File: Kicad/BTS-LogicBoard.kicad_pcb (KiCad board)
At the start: 2 copper layers, 41.9 x 55.9 mm, 54 parts, among them J1 Conn_01x06, J2 Conn_01x04, J3 Conn_01x02, Q1 BC817, Q2 BC807, Q3 BC817, Q4 BC807, Q5 BC817, Q6 BC817, SW1 SW_DPDT_x2, SW2 SW_DPDT_x2, U1 NCS2252SN2T1G, U2 NE555D, U3 NCS2252SN2T1G, U4 TLP291

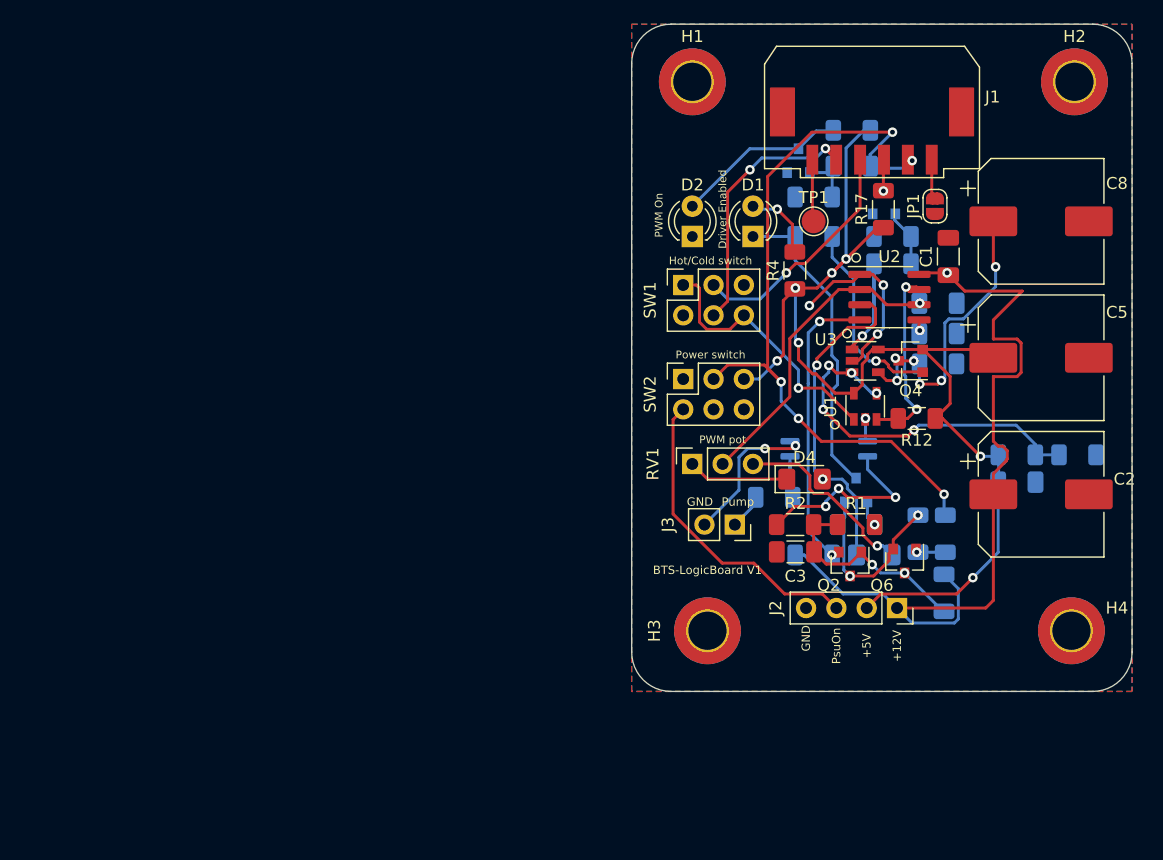
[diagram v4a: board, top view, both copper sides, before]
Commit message: Restarted layout
Signed-off-by: bebenlebricolo <benoittarrade@hotmail.fr>
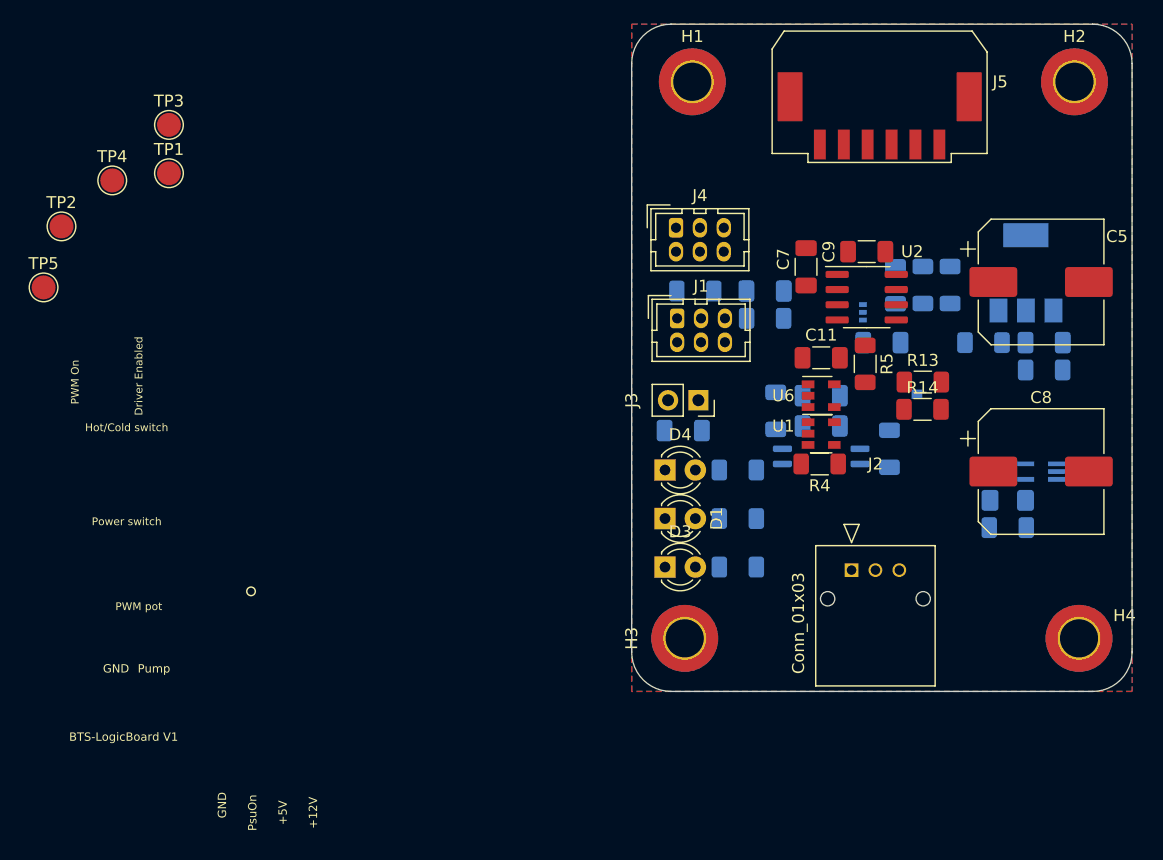
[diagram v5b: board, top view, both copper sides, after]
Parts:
- removed C1: 1uF, Capacitor_SMD:C_1206_3216Metric_Pad1.33x1.80mm_HandSolder
- removed C2: 470uF, Capacitor_SMD:CP_Elec_10x10
- removed JP1: SolderJumper_2_Open, Jumper:SolderJumper-2_P1.3mm_Open_RoundedPad1.0x1.5mm
- removed Q2, Q4: BC807, Package_TO_SOT_SMD:SOT-23
- removed Q3, Q5, Q6: BC817, Package_TO_SOT_SMD:SOT-23
- removed R17, R18: 1k, Resistor_SMD:R_1206_3216Metric_Pad1.30x1.75mm_HandSolder
- removed R19: 56k, Resistor_SMD:R_1206_3216Metric_Pad1.30x1.75mm_HandSolder
- removed RV1: R_POT, Connector_PinSocket_2.54mm:PinSocket_1x03_P2.54mm_Vertical
- removed SW1, SW2: SW_DPDT_x2, BTS-LogicBoard:PinSocket_2x03_P2.54mm_Vertical_DPDT_Special
- added C10: 100nF, Capacitor_SMD:C_1206_3216Metric_Pad1.33x1.80mm_HandSolder, B.Cu at (127.6, 99.7)
- added C11: 100nF, Capacitor_SMD:C_1206_3216Metric_Pad1.33x1.80mm_HandSolder, F.Cu at (127.6, 94.0)
- added C12: 100nF, Capacitor_SMD:C_1206_3216Metric_Pad1.33x1.80mm_HandSolder, B.Cu at (127.6, 97.2)
- added C13: 1uF, Capacitor_SMD:C_1206_3216Metric_Pad1.33x1.80mm_HandSolder, B.Cu at (122.9, 88.4)
- added C9: 100nF, Capacitor_SMD:C_1206_3216Metric_Pad1.33x1.80mm_HandSolder, F.Cu at (131.4, 85.1)
- added J4: Conn_02x03_Odd_Even, Connector_Hirose:Hirose_DF11-6DP-2DSA_2x03_P2.00mm_Vertical, F.Cu at (115.5, 83.1)
- added J5: Conn_01x06, BTS-LogicBoard:Molex_MicroLock_1.25_01x06, F.Cu at (136.5, 71.1)
- added TP2: TestPoint, TestPoint:TestPoint_Pad_D2.0mm, F.Cu at (64.0, 83.0)
- added TP3: TestPoint, TestPoint:TestPoint_Pad_D2.0mm, F.Cu at (73.0, 74.5)
- added TP4: TestPoint, TestPoint:TestPoint_Pad_D2.0mm, F.Cu at (68.3, 79.1)
- added TP5: TestPoint, TestPoint:TestPoint_Pad_D2.0mm, F.Cu at (62.5, 88.1)
- added U5: 74HC1GU04, Package_TO_SOT_SMD:SOT-353_SC-70-5, B.Cu at (130.2, 90.2)
- added U6: NCS2252SN2T1G, Package_TO_SOT_SMD:SOT-23-5, F.Cu at (127.6, 97.2)
- added U8: LM1117-5.0, Package_TO_SOT_SMD:SOT-223-3_TabPin2, B.Cu at (144.8, 86.9)
- C3, R2: moved to B.Cu
- C7: value 10pF -> 220pF; moved to F.Cu
- D2: value LED -> 1N4148; footprint LED_THT:LED_D3.0mm -> Diode_SMD:D_1206_3216Metric_Pad1.42x1.75mm_HandSolder; moved to B.Cu
- D3: value 1N4148 -> LED; footprint Diode_SMD:D_1206_3216Metric_Pad1.42x1.75mm_HandSolder -> LED_THT:LED_D3.0mm; moved to F.Cu
- D4: value 1N4148 -> LED; footprint Diode_SMD:D_1206_3216Metric_Pad1.42x1.75mm_HandSolder -> LED_THT:LED_D3.0mm
- J1: value Conn_01x06 -> Conn_02x03_Odd_Even; footprint BTS-LogicBoard:Molex_MicroLock_1.25_01x06 -> Connector_Hirose:Hirose_DF11-6DP-2DSA_2x03_P2.00mm_Vertical
- J2: value Conn_01x04 -> Conn_01x03; footprint Connector_PinSocket_2.54mm:PinSocket_1x04_P2.54mm_Vertical -> BTS-LogicBoard:559350310
- R1, R12: value 1k -> 470; moved to B.Cu
- R13: moved to F.Cu
- R14: value 390k -> 56k; moved to F.Cu
- R15: value 1k -> 470
- R16, R8: value 56k -> 5.6k
- R3: value 56k -> 390k
- R4: value 470 -> 1k
- R5: value 56k -> 1k; moved to F.Cu
- R6: value 1k -> 220
- R7: value 1k -> 10k
- U2: value NE555D -> NE555DR/TS555
- U3: value NCS2252SN2T1G -> 74HC1GU04; footprint Package_TO_SOT_SMD:SOT-23-5 -> Package_TO_SOT_SMD:SOT-353_SC-70-5_Handsoldering; moved to B.Cu
- moved TP1 54.1 mm to (73.0, 78.5)
- moved R9 37.8 mm to (120.7, 111.5)
- moved D2 34.4 mm to (143.3, 105.9), turned to 0 degrees
- moved J1 27.3 mm to (115.6, 90.7), turned to 0 degrees
- moved D1 24.7 mm to (114.6, 107.4), turned to 0 degrees
- moved R6 24.4 mm to (136.1, 87.9), turned to 90 degrees
- moved R15 21.6 mm to (120.7, 103.4)
- moved C8 21.0 mm to (146.1, 103.5)
- moved R5 20.3 mm to (131.3, 94.5)
- moved D3 17.6 mm to (114.6, 111.5)
- moved U3 17.4 mm to (146.1, 103.5), turned to 180 degrees
- moved R4 16.3 mm to (127.5, 102.9), turned to 180 degrees
- moved R13 15.2 mm to (136.1, 96.0), turned to 0 degrees
- moved C3 13.8 mm to (116.1, 100.1)
- moved R7 12.9 mm to (138.4, 87.9), turned to 90 degrees
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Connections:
- C3 pad 1: GND -> GND1
- C3 pad 2: /PWM_Enable -> /EnableSignal
- C4 pad 1: +5V -> VCC
- C5 pad 1: +5V -> VCC
- D1 pad 1: /PWM_Enabled_INV -> Net-(D1-Pad1)
- D2 pad 1: GND -> Net-(C8-Pad1)
- D2 pad 2: Net-(D2-Pad2) -> Net-(D1-Pad2)
- D3 pad 1: Net-(D3-Pad1) -> GND
- D4 pad 2: Net-(D3-Pad1) -> Net-(D4-Pad2)
- J1 pad 1: /HIP_HEN -> /+Potentiometer
- J1 pad 2: /HIP_DISABLE -> /PSU_ON
- J1 pad 3: /FAN_TRIGGER -> /PWM_DCycle_Ref
- J1 pad 4: /IN+ -> GND
- J1 pad 5: /IN- -> /-Potentiometer
- J1 pad 6: /VSense -> GND
- J2 pad 1: +12V -> +5V
- J2 pad 2: +5V -> /PSU_ON
- J2 pad 3: /PSU_ON -> GND
- J3 pad 1: /Pump-On -> /EnableSignal
- Q1 pad 3: /PWM_Enabled_INV -> Net-(D4-Pad1)
- R1 pad 1: Net-(Q1-Pad1) -> GND
- R1 pad 2: /PWM_Enable -> Net-(D1-Pad1)
- R10 pad 1: +5V -> VCC
- R12 pad 1: +5V -> VCC
- R12 pad 2: /NE-Out -> Net-(R12-Pad2)
- R13 pad 1: Net-(Q4-Pad1) -> /COMP_PWM
- R13 pad 2: /PWM_Enabled_INV -> Net-(Q1-Pad1)
- R14 pad 2: Net-(C8-Pad1) -> Net-(Q1-Pad1)
- R15 pad 1: Net-(Q5-Pad1) -> VCC
- R15 pad 2: /Inv_Fan_trigger -> Net-(D4-Pad2)
- R16 pad 1: GND -> /-Potentiometer
- R16 pad 2: Net-(Q5-Pad1) -> GND
- R2 pad 1: /PWM_Enable -> VCC
- R2 pad 2: Net-(R2-Pad2) -> /EnabledOpto
- R20 pad 2: /Pump-On -> /EnableSignal
- R3 pad 2: Net-(Q1-Pad1) -> Net-(C8-Pad1)
- R4 pad 1: +5V -> VCC
- R4 pad 2: Net-(D1-Pad2) -> /COMP_PWM
- R5 pad 1: +12V -> VCC
- R5 pad 2: /PWM_Enable -> /FAN_TRIGGER
- R6 pad 1: +12V -> Net-(R12-Pad2)
- R6 pad 2: Net-(Q2-Pad2) -> /Threshold
- R7 pad 1: Net-(Q3-Pad1) -> /Sawtooth
- R7 pad 2: /HIP_DISABLE -> /Threshold
- R8 pad 1: GND -> VCC
- R8 pad 2: Net-(Q3-Pad1) -> /+Potentiometer
- R9 pad 1: +5V -> VCC
- R9 pad 2: Net-(D2-Pad2) -> Net-(D3-Pad2)
- TP1 pad 1: /VSense -> /NE_OUT
- U1 pad 1: /COMP-Out -> /COMP_PWM
- U1 pad 3: /NE-Out -> /Sawtooth
- U1 pad 4: /2.5V -> /PWM_DCycle_Ref
- U1 pad 5: +5V -> VCC
- U2 pad 3: Net-(D3-Pad1) -> /NE_OUT
- U2 pad 4: Net-(Q2-Pad2) -> /NE555_RST
- U2 pad 7: /NE-Out -> Net-(R12-Pad2)
- U2 pad 8: +12V -> VCC
- U3 pad 1: /Inv_Fan_trigger -> (no net)
- U3 pad 2: GND -> /EnabledOpto
- U3 pad 3: /2.5V -> GND
- U3 pad 4: Net-(C8-Pad1) -> Net-(D1-Pad2)
- U3 pad 5: +5V -> VCC
- U4 pad 4: Net-(R2-Pad2) -> /EnabledOpto
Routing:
- net +5V: track 95.1 -> 0.00 mm, vias 7 -> 0
- net +12V: track 70.4 -> 0.00 mm, vias 1 -> 0
- net /HIP_DISABLE: track 64.7 -> 0.00 mm, vias 5 -> 0
- net GND: track 32.6 -> 0.00 mm, vias 6 -> 0
- net /2.5V: track 31.5 -> 0.00 mm, vias 5 -> 0
- net Net-(D3-Pad1): track 27.8 -> 0.00 mm, vias 2 -> 0
- net /PWM_Enabled_INV: track 26.4 -> 0.00 mm
- net /PSU_ON: track 26.1 -> 0.00 mm
- net /Threshold: track 25.9 -> 0.00 mm, vias 1 -> 0
- net Net-(C8-Pad1): track 25.2 -> 0.00 mm, vias 6 -> 0
- net Net-(Q2-Pad2): track 24.9 -> 0.00 mm, vias 2 -> 0
- net /COMP-Out: track 22.5 -> 0.00 mm, vias 1 -> 0
- net /IN-: track 21.8 -> 0.00 mm, vias 2 -> 0
- net /IN+: track 20.0 -> 0.00 mm, vias 1 -> 0
- net /PWM_Enable: track 18.3 -> 0.00 mm, vias 2 -> 0
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
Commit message: Finalized layout for Version 1.1 (need to work on silkscreen now)
Signed-off-by: bebenlebricolo <benoittarrade@hotmail.fr>
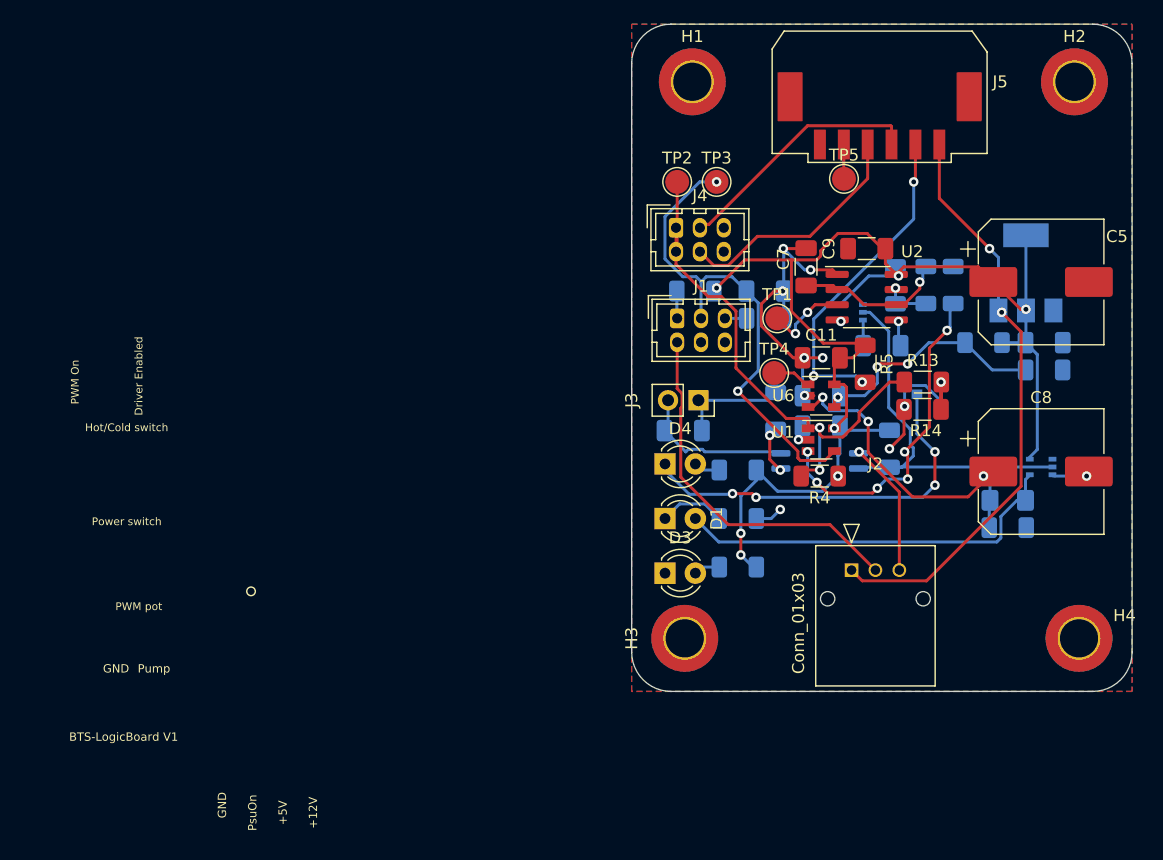
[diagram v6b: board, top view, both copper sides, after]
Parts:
- U3: footprint Package_TO_SOT_SMD:SOT-353_SC-70-5_Handsoldering -> Package_TO_SOT_SMD:SOT-353_SC-70-5
- moved TP5 67.6 mm to (129.5, 79.0)
- moved TP4 57.7 mm to (123.7, 95.2)
- moved TP1 52.4 mm to (124.0, 90.7)
- moved TP2 51.7 mm to (115.6, 79.2)
- moved TP3 46.1 mm to (118.9, 79.2)
- moved R4 1.02 mm to (127.5, 103.9)
- moved D3 0.51 mm to (114.6, 112.0)
- moved D4 0.51 mm to (114.6, 102.9)
- moved U1 0.51 mm to (127.6, 100.8)
- moved U4 0.40 mm to (127.5, 102.6)
- moved U3 0.38 mm to (146.1, 103.1)
- moved C6 0.25 mm to (132.7, 93.0)
- moved C9 0.25 mm to (131.4, 84.8)
- moved R6 0.25 mm to (136.4, 87.9)
- moved R7 0.25 mm to (138.7, 87.9)
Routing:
- net VCC: track 0.00 -> 108.6 mm, vias 0 -> 7
- net GND: track 0.00 -> 59.1 mm, vias 0 -> 12
- net +5V: track 0.00 -> 49.4 mm, vias 0 -> 2
- net /COMP_PWM: track 0.00 -> 45.3 mm, vias 0 -> 2
- net /PWM_DCycle_Ref: track 0.00 -> 41.1 mm, vias 0 -> 2
- net Net-(D1-Pad2): track 0.00 -> 33.1 mm
- net /EnabledOpto: track 0.00 -> 32.8 mm
- net Net-(D4-Pad1): track 0.00 -> 32.3 mm, vias 0 -> 4
- net /FAN_TRIGGER: track 0.00 -> 31.3 mm, vias 0 -> 3
- net /PSU_ON: track 0.00 -> 31.0 mm
- net /Sawtooth: track 0.00 -> 28.0 mm, vias 0 -> 6
- net Net-(C8-Pad1): track 0.00 -> 27.6 mm, vias 0 -> 3
- net /IN+: track 0.00 -> 21.1 mm
- net /IN-: track 0.00 -> 20.4 mm
- net /2.5V: track 0.00 -> 20.3 mm, vias 0 -> 3
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
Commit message: Finalized board layout with silkscreen
Signed-off-by: bebenlebricolo <benoittarrade@hotmail.fr>
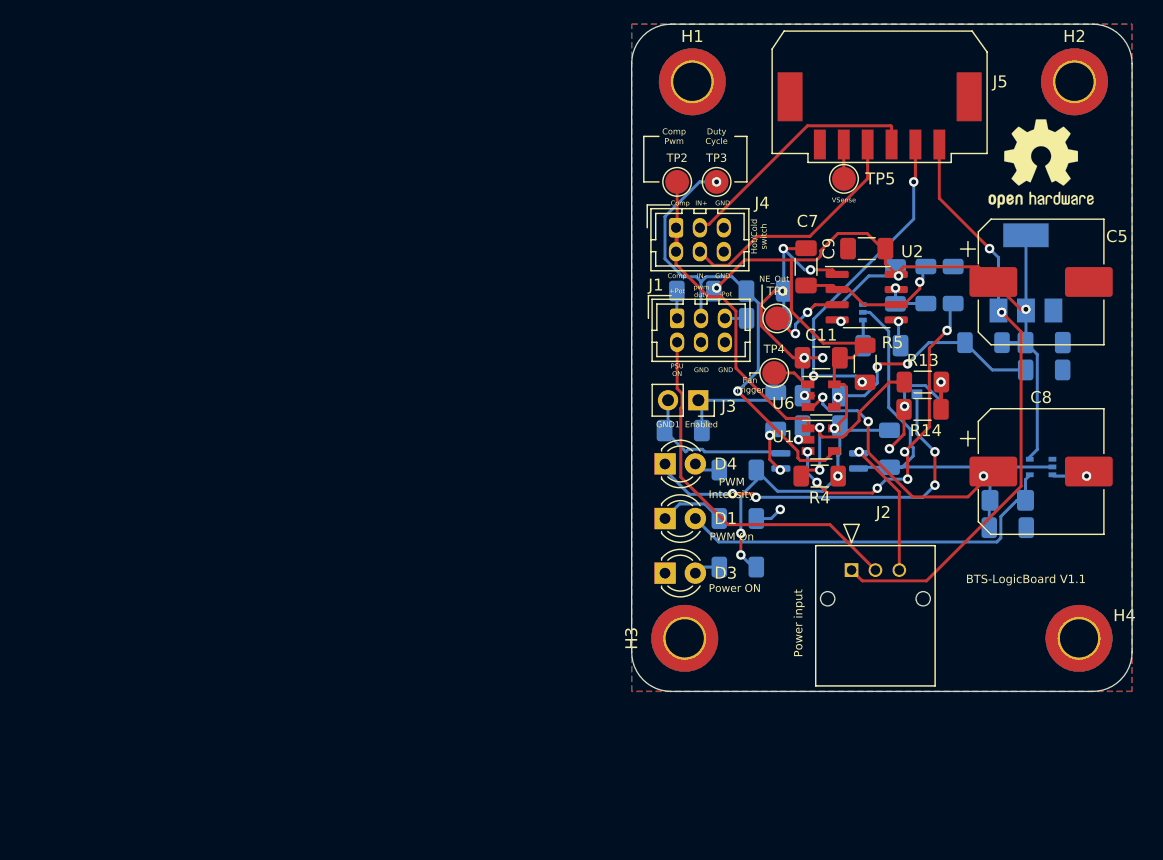
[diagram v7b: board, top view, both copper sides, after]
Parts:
- added REF**: OSHW-Logo2_9.8x8mm_SilkScreen, Symbol:OSHW-Logo2_9.8x8mm_SilkScreen, F.Cu at (146.1, 77.7)
- J2: value Conn_01x03 -> Power input
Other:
- board text added: "+Pot"
- board text added: "-Pot"
- board text added: "BTS-LogicBoard V1.1"
- board text added: "Comp"
- board text added: "Comp Pwm"
- board text added: "Duty Cycle"
- board text added: "Enabled"
- board text added: "Fan Trigger"
- board text added: "GND1"
- board text added: "IN+"
- board text added: "IN-"
- board text added: "NE_Out"
- board text added: "PSU ON"
- board text added: "PWM Intensity"
- board text added: "Power ON"
- board text added: "VSense"
- board text added: "pwm duty"
- board text removed: "+12V"
- board text removed: "+5V"
- board text removed: "BTS-LogicBoard V1"
- board text removed: "Driver Enabled"
- board text removed: "PWM pot"
- board text removed: "Power switch"
- board text removed: "PsuOn"
- board text removed: "Pump"

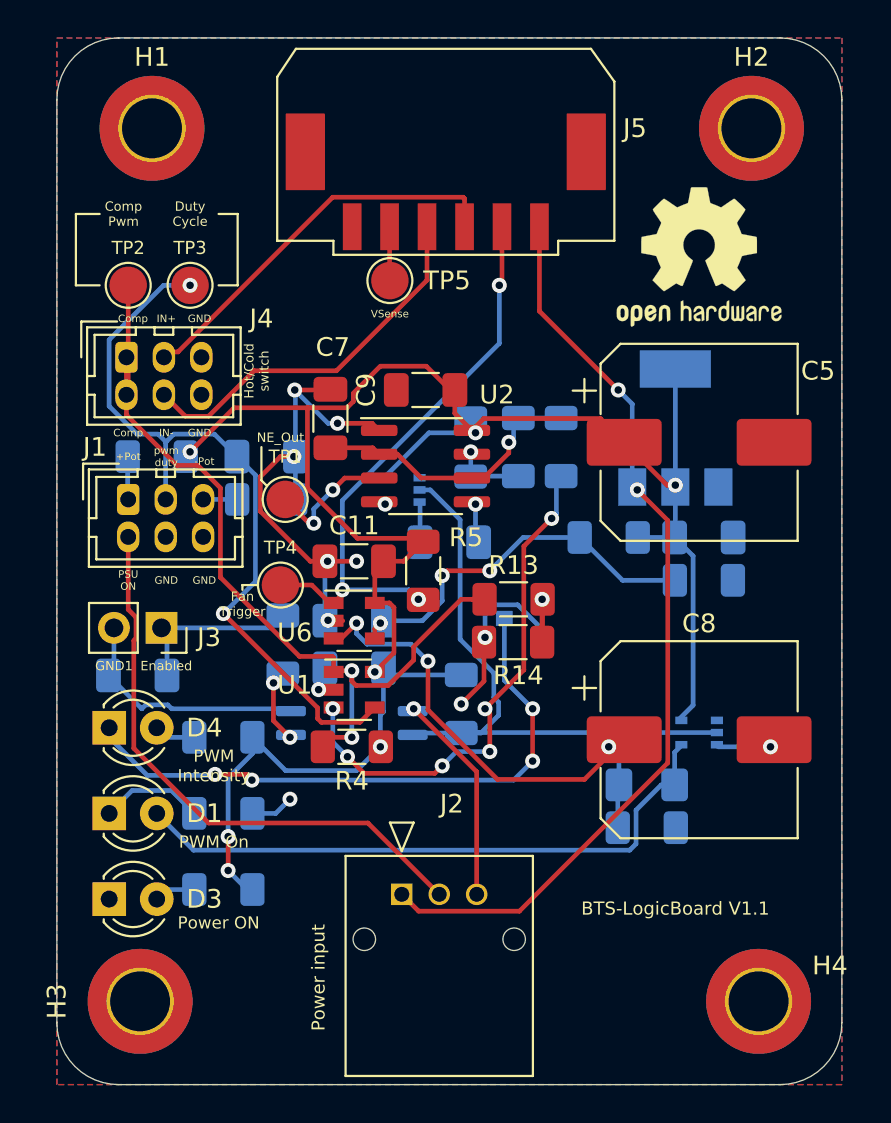
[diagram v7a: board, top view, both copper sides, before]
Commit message: Added hysteresis resistor to comparators and reexported gerbers
Signed-off-by: bebenlebricolo <benoittarrade@hotmail.fr>
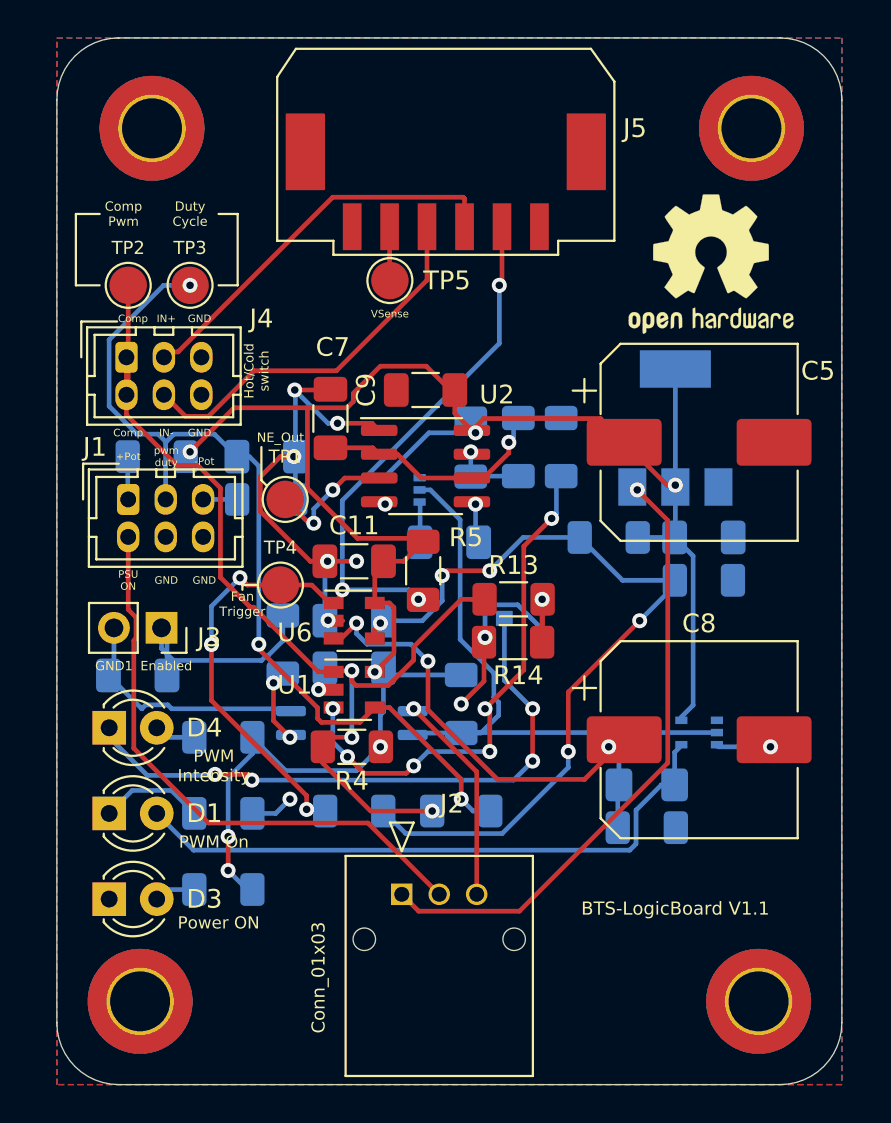
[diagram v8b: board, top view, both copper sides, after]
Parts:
- added R17: 56k, Resistor_SMD:R_1206_3216Metric_Pad1.30x1.75mm_HandSolder, B.Cu at (133.3, 107.3)
- added R18: 56k, Resistor_SMD:R_1206_3216Metric_Pad1.30x1.75mm_HandSolder, B.Cu at (127.6, 107.3)
- added REF**: KiCad-Logo2_5mm_SilkScreen, Symbol:KiCad-Logo2_5mm_SilkScreen, B.Cu at (132.1, 71.1)
- J2: value Power input -> Conn_01x03
- moved REF** 0.74 mm to (146.7, 78.1)
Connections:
- J5 pad 1: +5V -> (no net)
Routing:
- net /2.5V: track 20.3 -> 44.5 mm, vias 3 -> 5
- net /FAN_TRIGGER: track 31.3 -> 49.8 mm, vias 3 -> 6
- net +5V: track 49.4 -> 33.4 mm, vias 2 -> 1
- net /PWM_DCycle_Ref: track 41.1 -> 49.1 mm, vias 2 -> 3
- net /COMP_PWM: track 45.3 -> 52.6 mm, vias 2 -> 3
- net /EnableSignal: track 9.41 -> 12.3 mm
